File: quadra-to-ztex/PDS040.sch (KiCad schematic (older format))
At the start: 11 parts, among them IC1 74CB3T16211DGGR, IC2 74CB3T16211DGGR, IC3 74CB3T16211DGGR, IC4 74CB3T16211DGGR, U14 8807-140-170LH

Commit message: length tuning
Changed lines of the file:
@@
 Text GLabel 4325 1475 2    50   Input ~ 0
 ~TBI
-Text Notes 4525 1475 0    50   ~ 0
-needed?
 Text GLabel 4325 1275 2    50   Input ~ 0
 ~TA
@@
 Text GLabel 9425 975  2    50   Input ~ 0
 SC0
-Text Notes 9625 1100 0    50   ~ 0
-needed?
-Text Notes 9625 975  0    50   ~ 0
-needed?
 Text GLabel 8000 2400 2    50   Input ~ 0
 ~TRST
@@
 Text GLabel 10025 1825 2    50   Input ~ 0
 ~ANALOGRESET
-Text Notes 4575 5550 0    50   ~ 0
-needed?
 Text GLabel 4325 5550 2    50   Input ~ 0
 ~RSTQ
@@
 Text Notes 9325 850  0    50   ~ 0
 Snooping
+Text Notes 9625 1000 0    50   ~ 0
+not needed
+Text Notes 9625 1100 0    50   ~ 0
+not needed
 $EndSCHEMATC

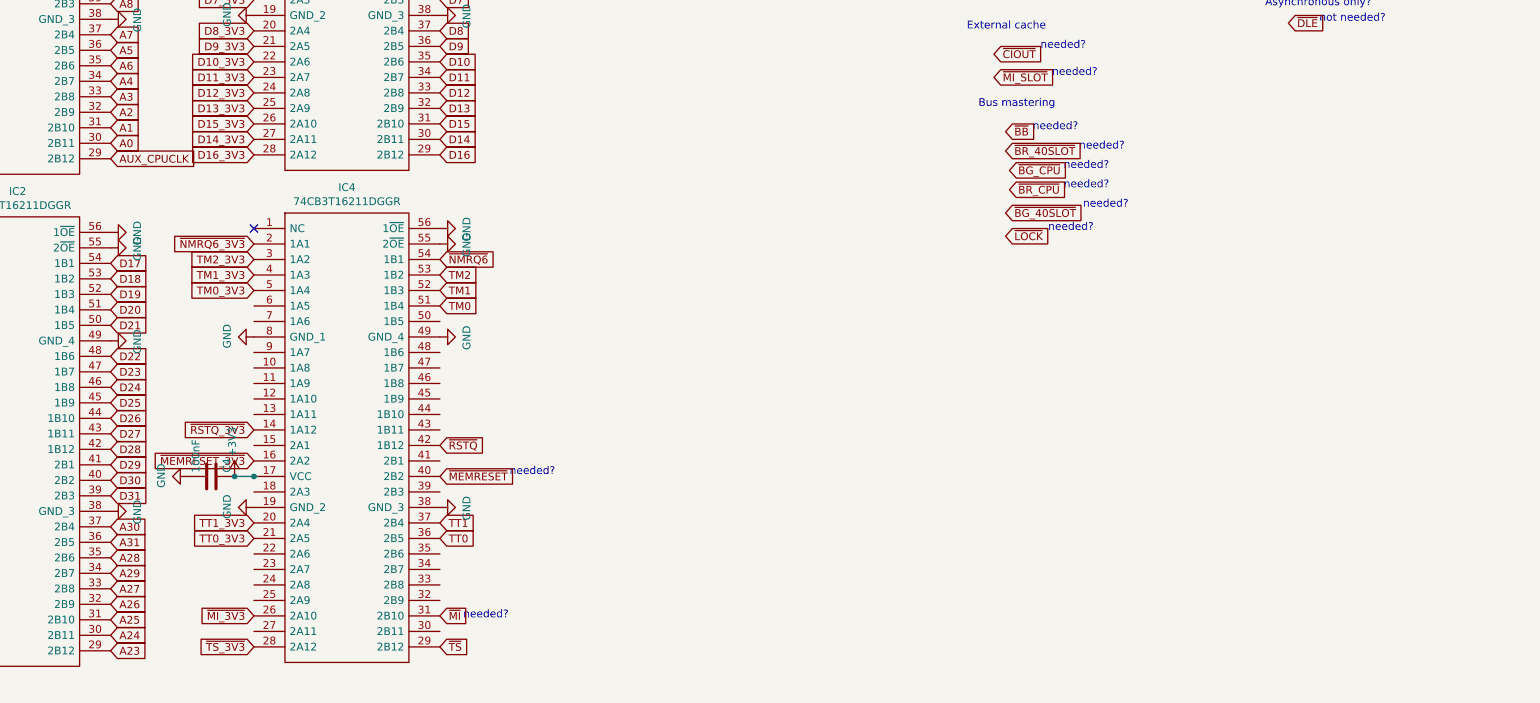
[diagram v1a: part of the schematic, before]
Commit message: remove memreset, add busmastering (?)
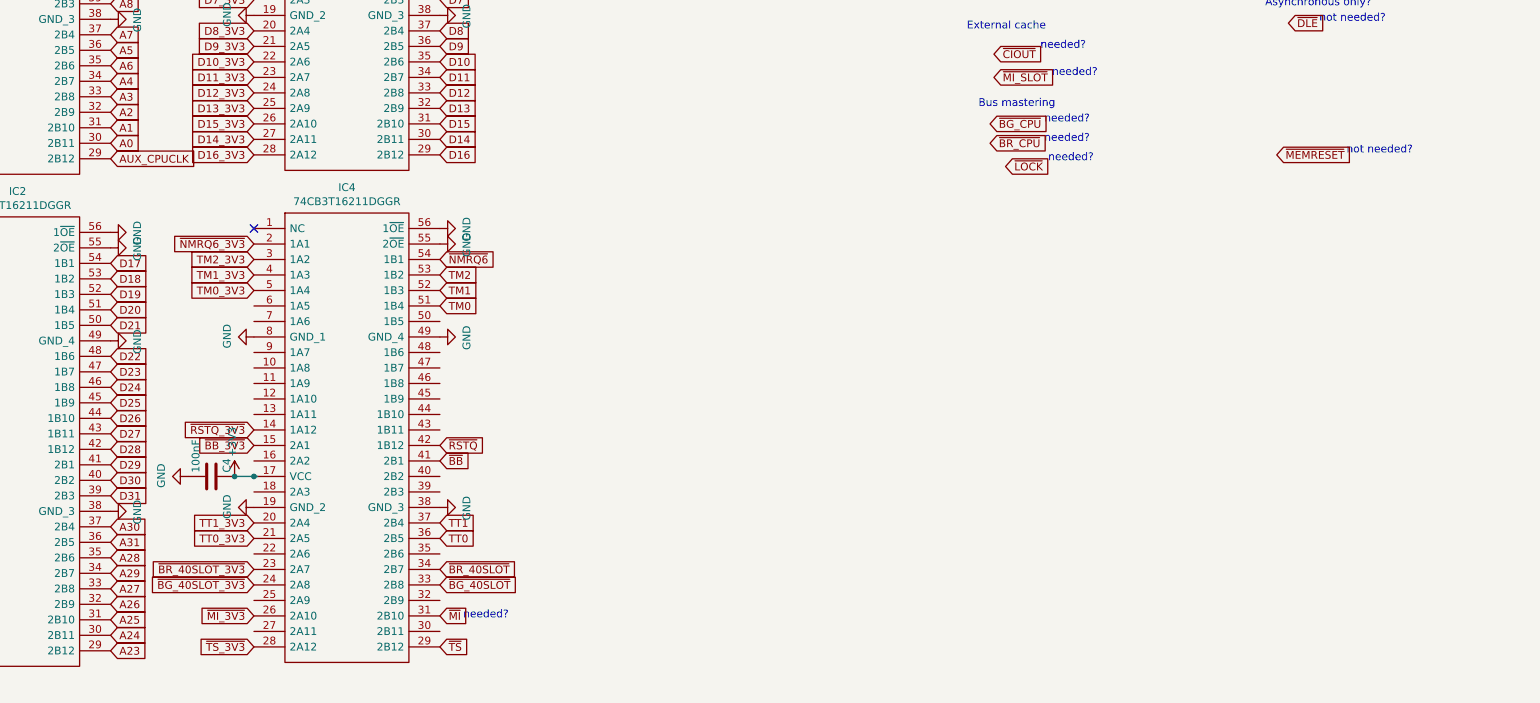
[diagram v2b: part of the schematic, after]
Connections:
- net labels added: ~BB_3V3, ~BG_40SLOT_3V3, ~BR_40SLOT_3V3
- net labels removed: ~MEMRESET_3V3
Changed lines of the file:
@@
 Text Notes 8275 3175 0    50   ~ 0
 needed?
-Text GLabel 7975 4050 2    50   Input ~ 0
+Text GLabel 4325 6450 2    50   Input ~ 0
 ~BG_40SLOT
-Text Notes 8475 4025 0    50   ~ 0
+Text GLabel 7875 3600 2    50   Input ~ 0
+~BR_CPU
+Text GLabel 7875 3475 2    50   Input ~ 0
+~BG_CPU
+Text GLabel 4325 6350 2    50   Input ~ 0
+~BR_40SLOT
+Text Notes 8225 3600 0    50   ~ 0
 needed?
-Text GLabel 8000 3900 2    50   Input ~ 0
-~BR_CPU
-Text GLabel 8000 3775 2    50   Input ~ 0
-~BG_CPU
-Text GLabel 7975 3650 2    50   Input ~ 0
-~BR_40SLOT
-Text Notes 8350 3900 0    50   ~ 0
+Text Notes 8225 3475 0    50   ~ 0
 needed?
-Text Notes 8350 3775 0    50   ~ 0
-needed?
-Text Notes 8450 3650 0    50   ~ 0
-needed?
-Text GLabel 7975 3525 2    50   Input ~ 0
+Text GLabel 4325 5650 2    50   Input ~ 0
 ~BB
-Text Notes 8150 3525 0    50   ~ 0
-needed?
 Text GLabel 4325 6150 2    50   Input ~ 0
 TT0
-Text GLabel 7975 4200 2    50   Input ~ 0
+Text GLabel 7975 3750 2    50   Input ~ 0
 ~LOCK
 Text GLabel 4325 6050 2    50   Input ~ 0
 TT1
-Text Notes 8250 4175 0    50   ~ 0
+Text Notes 8250 3725 0    50   ~ 0
 needed?
-Text GLabel 4325 5750 2    50   Input ~ 0
+Text GLabel 9725 3675 2    50   Input ~ 0
 ~MEMRESET
-Text Notes 4775 5750 0    50   ~ 0
-needed?
+Text Notes 10175 3675 0    50   ~ 0
+not needed?
 Text GLabel 7900 1075 2    50   Input ~ 0
 TLN0
@@
 Text GLabel 3125 6050 0    50   Input ~ 0
 TT1_3V3
-Text GLabel 3125 5650 0    50   Input ~ 0
-~MEMRESET_3V3
 Text GLabel 3125 5450 0    50   Input ~ 0
 ~RSTQ_3V3
@@
 Text Notes 9625 1100 0    50   ~ 0
 not needed
+Text GLabel 3125 6450 0    50   Input ~ 0
+~BG_40SLOT_3V3
+Text GLabel 3125 6350 0    50   Input ~ 0
+~BR_40SLOT_3V3
+Text GLabel 3125 5550 0    50   Input ~ 0
+~BB_3V3
 $EndSCHEMATC

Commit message: oups A5
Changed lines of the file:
@@
 Text GLabel 14175 7150 2    50   Input ~ 0
 A3
-Text GLabel 12675 6850 0    50   Input ~ 0
+Text GLabel 12675 6950 0    50   Input ~ 0
 A5
 Text GLabel 14175 6850 2    50   Input ~ 0
@@
 L power:GND #PWR0141
 U 1 1 6447C6EC
-P 12675 6950
-F 0 "#PWR0141" H 12675 6700 50  0001 C CNN
-F 1 "GND" V 12680 6822 50  0000 R CNN
-F 2 "" H 12675 6950 50  0001 C CNN
-F 3 "" H 12675 6950 50  0001 C CNN
-	1    12675 6950
+P 12675 6850
+F 0 "#PWR0141" H 12675 6600 50  0001 C CNN
+F 1 "GND" V 12680 6722 50  0000 R CNN
+F 2 "" H 12675 6850 50  0001 C CNN
+F 3 "" H 12675 6850 50  0001 C CNN
+	1    12675 6850
 	0    1    1    0
 $EndComp

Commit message: oups wrong pin
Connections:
- wire segments 8 -> 4
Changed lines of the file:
@@
 	1    0    0    -1
 $EndComp
-Wire Wire Line
-	1025 2600 1000 2600
 Connection ~ 875  2600
-Connection ~ 1000 2600
 Wire Wire Line
 	1000 2600 875  2600
@@
 	1    0    0    -1
 $EndComp
-Wire Wire Line
-	1025 5775 1000 5775
 Connection ~ 875  5775
-Connection ~ 1000 5775
 Wire Wire Line
 	1000 5775 875  5775
@@
 	1    0    0    -1
 $EndComp
-Wire Wire Line
-	3150 2575 3125 2575
-Connection ~ 3000 2575
-Connection ~ 3125 2575
-Wire Wire Line
-	3125 2575 3000 2575
 $Comp
 L power:GND #PWR0120
@@
 Text GLabel 6350 1450 0    50   Input ~ 0
 ~PDS_SLOT_E_EN
-NoConn ~ 14775 2750
+NoConn ~ 12725 2825
 Text GLabel 2200 3700 2    50   Input ~ 0
 AUX_CPUCLK
@@
 	1    0    0    -1
 $EndComp
-Wire Wire Line
-	3150 5750 3125 5750
 Connection ~ 3000 5750
-Connection ~ 3125 5750
 Wire Wire Line
 	3125 5750 3000 5750
@@
 Text GLabel 3125 5550 0    50   Input ~ 0
 ~BB_3V3
+Wire Wire Line
+	3125 2575 3000 2575
+Connection ~ 3000 2575
 $EndSCHEMATC

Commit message: regen
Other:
- note added: "ATTN:\n"Devices that transfer data on the system bus,\nsuch as PDS bus masters, must drive the snoop\ncontrol pins (SCO and SCl) to indicate no snooping""
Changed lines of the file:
@@
 	3125 2575 3000 2575
 Connection ~ 3000 2575
+Text Notes 10325 1375 2    50   ~ 0
+ATTN:\n"Devices that transfer data on the system bus,\nsuch as PDS bus masters, must drive the snoop\ncontrol pins (SCO and SCl) to indicate no snooping"
 $EndSCHEMATC

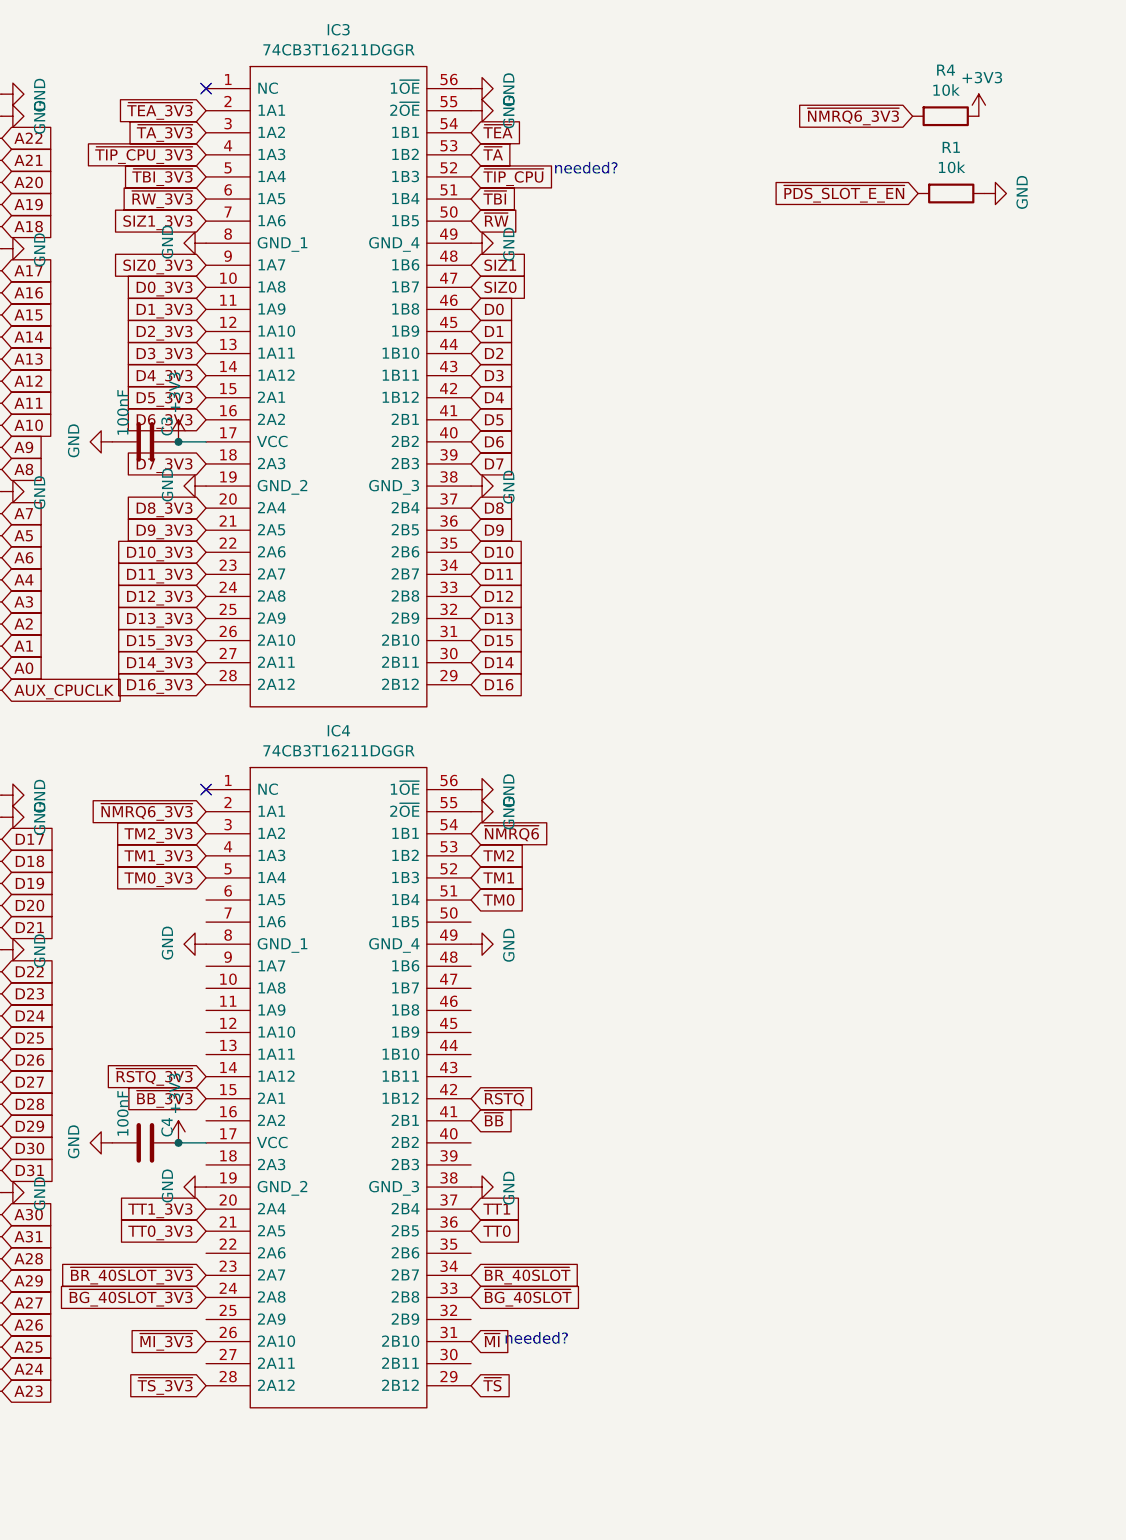
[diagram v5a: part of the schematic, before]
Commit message: R1 must be 0 ohm (there's a pull-up on the motherboard and it's stronger)
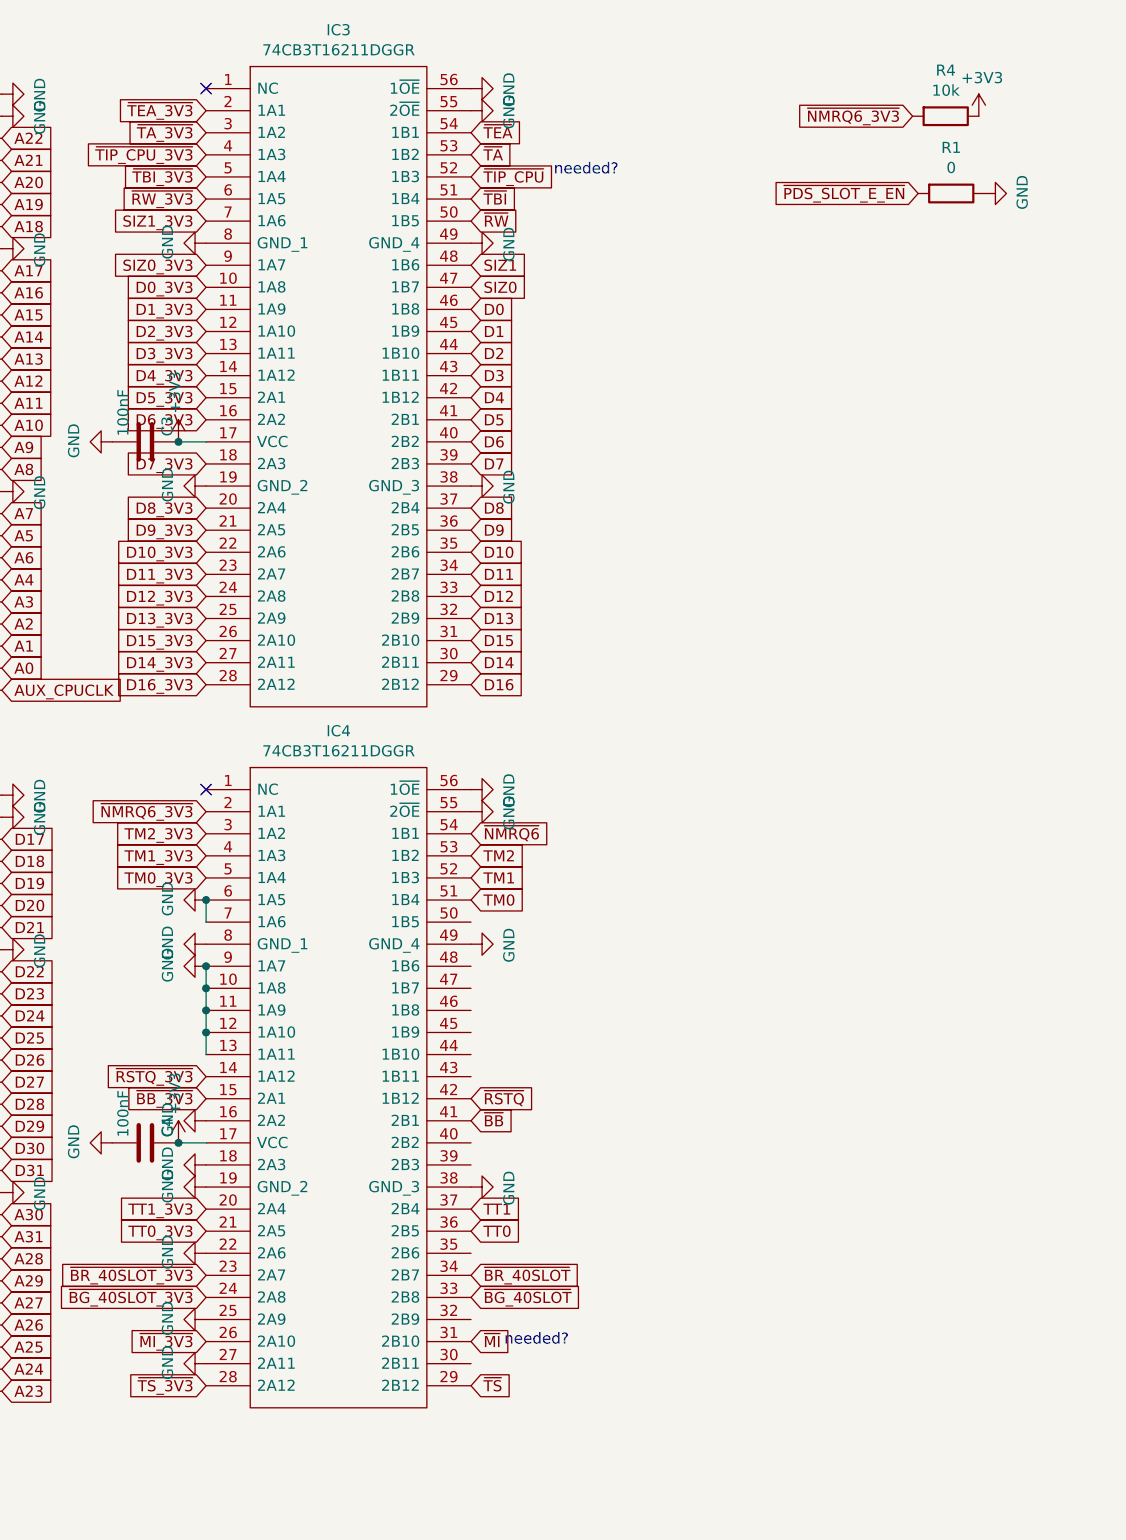
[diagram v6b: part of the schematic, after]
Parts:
- R1: value 10k -> 0; MPN 0402WGF1002TCE -> 0402WGF0000TCE
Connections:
- net GND: now also IC4.10 (1A8), IC4.11 (1A9), IC4.12 (1A10), IC4.13 (1A11), IC4.16 (2A2), IC4.18 (2A3), IC4.22 (2A6), IC4.25 (2A9), IC4.27 (2A11), IC4.6 (1A5), IC4.7 (1A6), IC4.9 (1A7)
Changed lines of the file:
@@
 P 6500 1450
 F 0 "R1" V 6293 1450 50  0000 C CNN
-F 1 "10k" V 6384 1450 50  0000 C CNN
+F 1 "0" V 6384 1450 50  0000 C CNN
 F 2 "Resistor_SMD:R_0402_1005Metric" V 6430 1450 50  0001 C CNN
 F 3 "~" H 6500 1450 50  0001 C CNN
-F 4 "0402WGF1002TCE" V 6500 1450 50  0001 C CNN "MPN"
+F 4 "0402WGF0000TCE" V 6500 1450 50  0001 C CNN "MPN"
 	1    6500 1450
 	0    1    1    0
@@
 Text Notes 10325 1375 2    50   ~ 0
 ATTN:\n"Devices that transfer data on the system bus,\nsuch as PDS bus masters, must drive the snoop\ncontrol pins (SCO and SCl) to indicate no snooping"
+Wire Wire Line
+	3125 4650 3125 4750
+Wire Wire Line
+	3125 4950 3125 5050
+Connection ~ 3125 5050
+Wire Wire Line
+	3125 5050 3125 5150
+Connection ~ 3125 5150
+Wire Wire Line
+	3125 5150 3125 5250
+Connection ~ 3125 5250
+Wire Wire Line
+	3125 5250 3125 5350
+$Comp
+L power:GND #PWR?
+U 1 1 65E4D5E1
+P 3125 4650
+F 0 "#PWR?" H 3125 4400 50  0001 C CNN
+F 1 "GND" H 3130 4477 50  0000 C CNN
+F 2 "" H 3125 4650 50  0001 C CNN
+F 3 "" H 3125 4650 50  0001 C CNN
+	1    3125 4650
+	0    1    -1   0
+$EndComp
+Connection ~ 3125 4650
+$Comp
+L power:GND #PWR?
+U 1 1 65E4D743
+P 3125 4950
+F 0 "#PWR?" H 3125 4700 50  0001 C CNN
+F 1 "GND" H 3130 4777 50  0000 C CNN
+F 2 "" H 3125 4950 50  0001 C CNN
+F 3 "" H 3125 4950 50  0001 C CNN
+	1    3125 4950
+	0    1    -1   0
+$EndComp
+Connection ~ 3125 4950
+$Comp
+L power:GND #PWR?
+U 1 1 65E4D996
+P 3125 5650
+F 0 "#PWR?" H 3125 5400 50  0001 C CNN
+F 1 "GND" H 3130 5477 50  0000 C CNN
+F 2 "" H 3125 5650 50  0001 C CNN
+F 3 "" H 3125 5650 50  0001 C CNN
+	1    3125 5650
+	0    1    -1   0
+$EndComp
+$Comp
+L power:GND #PWR?
+U 1 1 65E4DC41
+P 3125 5850
+F 0 "#PWR?" H 3125 5600 50  0001 C CNN
+F 1 "GND" H 3130 5677 50  0000 C CNN
+F 2 "" H 3125 5850 50  0001 C CNN
+F 3 "" H 3125 5850 50  0001 C CNN
+	1    3125 5850
+	0    1    -1   0
+$EndComp
+$Comp
+L power:GND #PWR?
+U 1 1 65E4DEBC
+P 3125 6250
+F 0 "#PWR?" H 3125 6000 50  0001 C CNN
+F 1 "GND" H 3130 6077 50  0000 C CNN
+F 2 "" H 3125 6250 50  0001 C CNN
+F 3 "" H 3125 6250 50  0001 C CNN
+	1    3125 6250
+	0    1    -1   0
+$EndComp
+$Comp
+L power:GND #PWR?
+U 1 1 65E4E1A4
+P 3125 6550
+F 0 "#PWR?" H 3125 6300 50  0001 C CNN
+F 1 "GND" H 3130 6377 50  0000 C CNN
+F 2 "" H 3125 6550 50  0001 C CNN
+F 3 "" H 3125 6550 50  0001 C CNN
+	1    3125 6550
+	0    1    -1   0
+$EndComp
+$Comp
+L power:GND #PWR?
+U 1 1 65E4E3F8
+P 3125 6750
+F 0 "#PWR?" H 3125 6500 50  0001 C CNN
+F 1 "GND" H 3130 6577 50  0000 C CNN
+F 2 "" H 3125 6750 50  0001 C CNN
+F 3 "" H 3125 6750 50  0001 C CNN
+	1    3125 6750
+	0    1    -1   0
+$EndComp
 $EndSCHEMATC
